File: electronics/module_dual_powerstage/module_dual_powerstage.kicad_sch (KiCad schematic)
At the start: 2 parts

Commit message: Schematic and layout done, review needed
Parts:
- added C1: 1u, SquantorCapacitor:C_0805+0603, symbol Device:C
- added J1, J2: Conn_01x04, SquantorConnectors:Header-0254-1X04-H010, symbol Connector_Generic:Conn_01x04
- N2: renamed from N1; value 20231214 -> 20250926
- renumbered N2 to N1
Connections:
- new net AC1_IN: J1.1 (Pin_1)
- new net AC1_OUT: J1.2 (Pin_2)
- new net AC2_IN: J1.3 (Pin_3)
- new net AC2_OUT: J1.4 (Pin_4)
- new net GND: C1.2, J2.4 (Pin_4)
- new net SW1: J2.2 (Pin_2)
- new net SW2: J2.1 (Pin_1)
- new net V3.3: C1.1, J2.3 (Pin_3)
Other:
- added sheet dual_nmos_switch (dual_nmos_switch.kicad_sch)
- note added: "Connections"
- note added: "Powersupply"

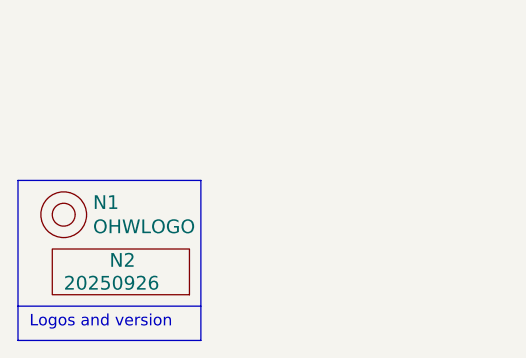
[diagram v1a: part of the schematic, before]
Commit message: ERC/DRC fixes, headers better aligned
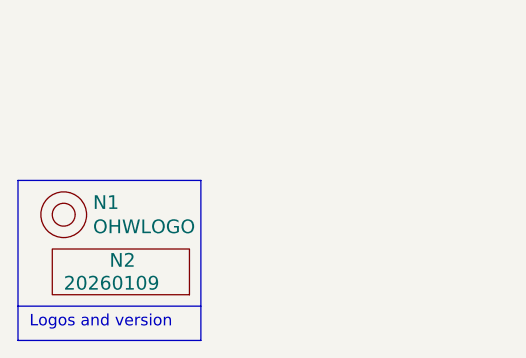
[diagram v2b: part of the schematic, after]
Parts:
- N2: value 20250926 -> 20260109
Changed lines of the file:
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@@
 			)
 		)
-		(property "Value" "20250926"
+		(property "Value" "20260109"
 			(at 20.32 189.23 0)
 			(effects

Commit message: preparation for production
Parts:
- N2: value 20260109 -> 20260118
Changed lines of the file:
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@@
 			)
 		)
-		(property "Value" "20260109"
+		(property "Value" "20260118"
 			(at 20.32 189.23 0)
 			(effects
